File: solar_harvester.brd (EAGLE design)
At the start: 100 x 80 mm, 63 parts, among them U1 BQ25505, U2 TPS61322XA, U3 TPS61322XA, U4 MAX17040, U5 INA226

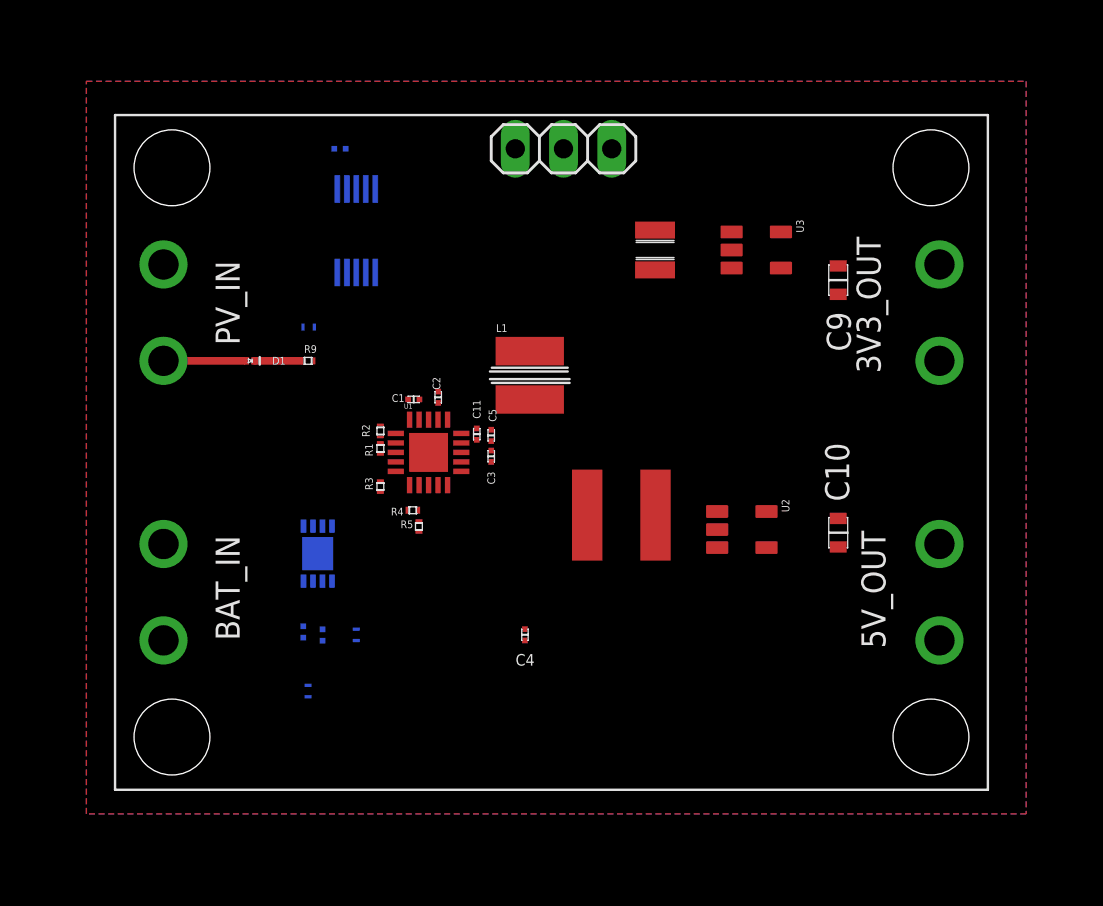
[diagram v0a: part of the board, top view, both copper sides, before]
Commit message: bq25505, both tps622, max17004 routed
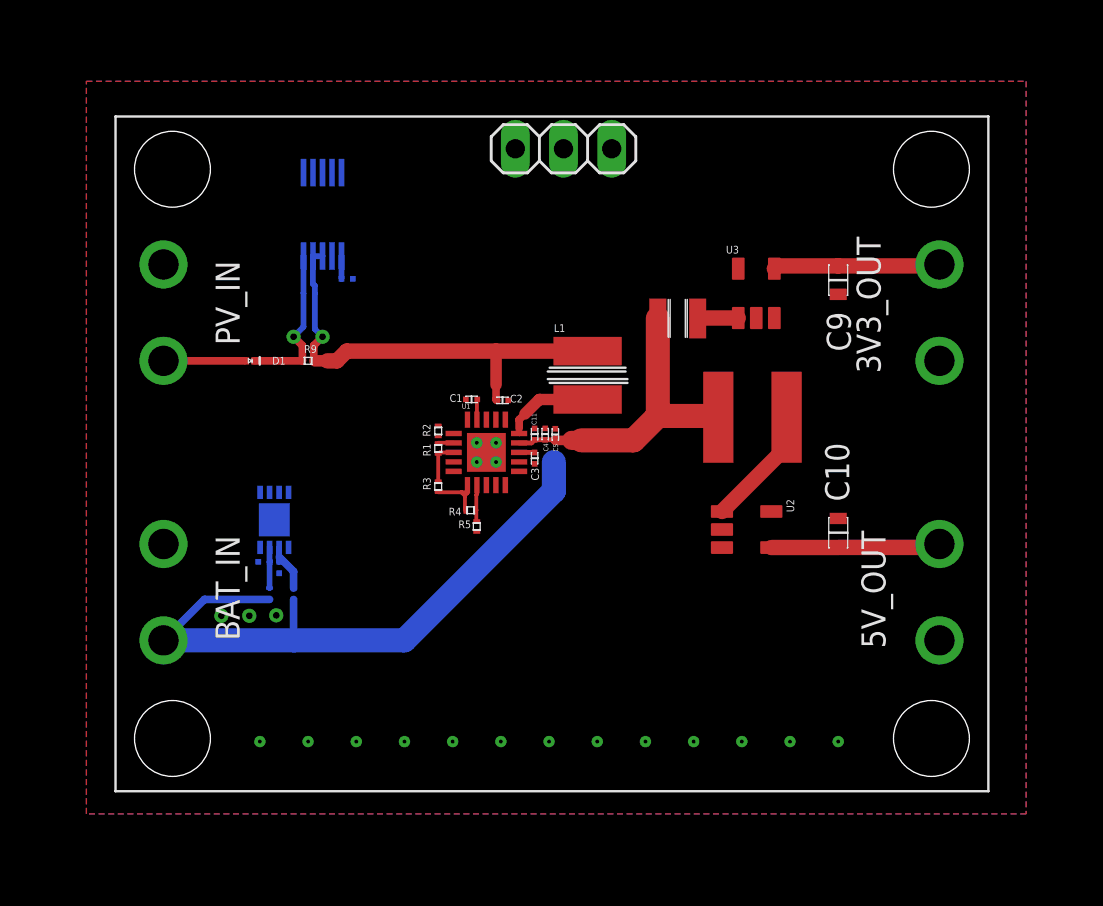
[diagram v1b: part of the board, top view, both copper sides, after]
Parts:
- added U$29: LOUT, vrlib_com_symbols:LOUT_FOOTPRINT
- C11: value 4u7 -> 10u
- C4: value 10u -> 4u7
- moved C4 10.6 mm to (35.4, 31.4)
- moved L2 8.62 mm to (46.3, 32.3)
- moved C8 6.87 mm to (24.9, 39.6)
- moved R7 5.52 mm to (20.8, 23.0)
- moved C7 4.24 mm to (20.5, 24.7), turned to 90 degrees
- moved C6 4.23 mm to (21.3, 24.4)
- moved R6 3.95 mm to (22.1, 23.0)
- moved L3 3.80 mm to (42.3, 37.5), turned to 90 degrees
- moved C2 3.39 mm to (33.1, 33.2), turned to 90 degrees
- moved C5 3.38 mm to (35.9, 31.4)
- moved C11 3.05 mm to (34.8, 31.4)
- moved L1 3.05 mm to (37.6, 34.5)
- moved R4 3.05 mm to (31.4, 27.4)
- moved U1 3.05 mm to (32.3, 30.5)
- moved C1 3.05 mm to (31.5, 33.3)
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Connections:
- removed net GND1: C6.2, C7.2, C8.2, U4.1, U4.4, U4.5, U4.6, U4.9, U5.1, U5.2, U5.7
- removed net VSTOR: C11.1, C5.1, C8.1, U1.19, U1.3, U5.6
- new net VCC: C11.1, C4.1, C5.1, C8.1, L2.1, L3.1, U1.19, U1.3, U5.6
- net GND: now also C6.2, C7.2, C8.2, U4.1, U4.4, U4.5, U4.6, U4.9, U5.1, U5.2, U5.7
- net VIN_BAT: no longer C4.1, L2.1, L3.1
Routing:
- net VIN_BAT: track 0.00 -> 34.8 mm
- net PVIN_AN: track 0.00 -> 23.6 mm, vias 0 -> 1
- net VCC: track 0.00 -> 17.5 mm
- net VDD3V3: track 0.00 -> 8.69 mm
- net VDD5: track 0.00 -> 8.60 mm
- net PVIN: track 2.55 -> 8.48 mm, vias 0 -> 1
- net N$11: track 0.00 -> 5.76 mm
- net N$1: track 0.00 -> 4.77 mm
- net N$5: track 0.00 -> 3.19 mm
- net N$8: track 0.00 -> 2.71 mm
- net N$3: track 0.00 -> 2.26 mm
- net N$10: track 0.00 -> 2.15 mm
- net N$7: track 0.00 -> 2.14 mm
- net N$6: track 0.00 -> 1.90 mm
- net N$2: track 0.00 -> 1.08 mm
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- added copper zone on layer 16, net GND
- removed copper zone on layer 16, net GND2

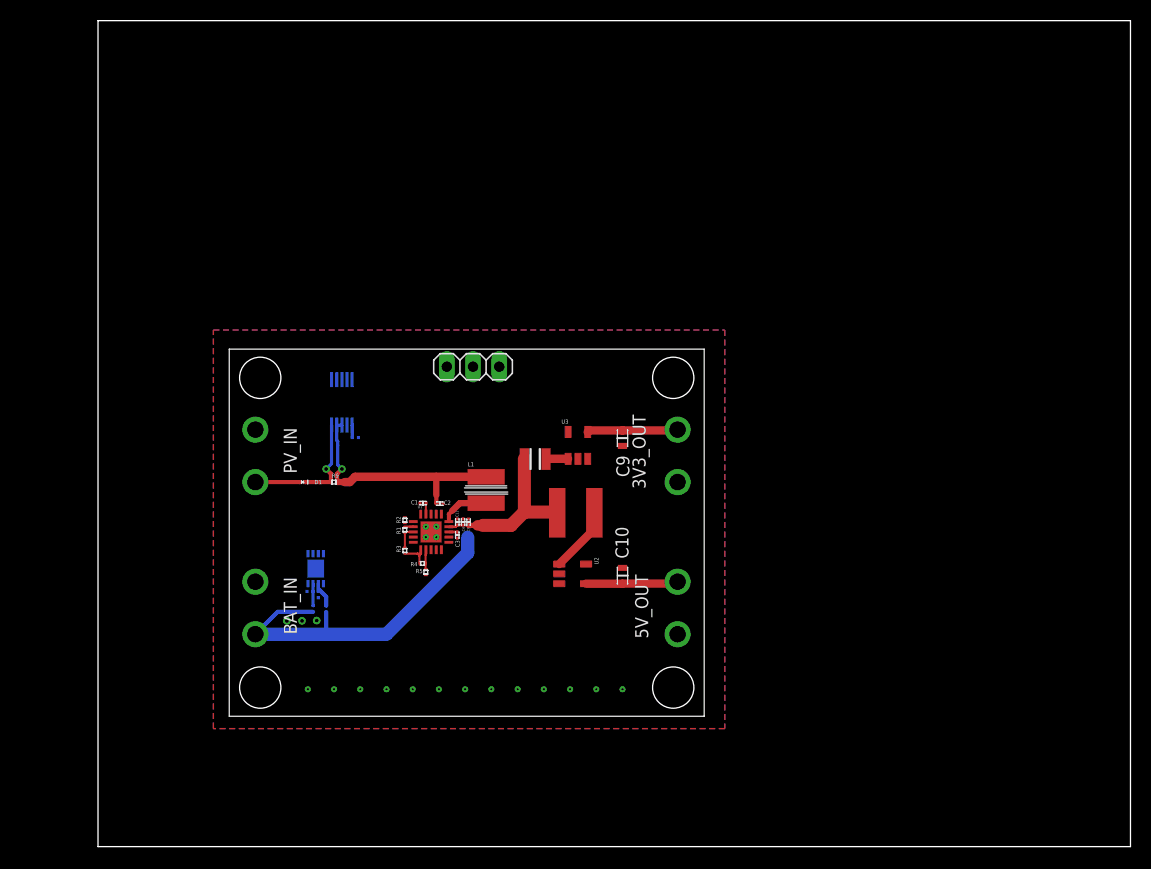
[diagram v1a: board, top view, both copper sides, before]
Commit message: routing complete without battery under-voltage protection
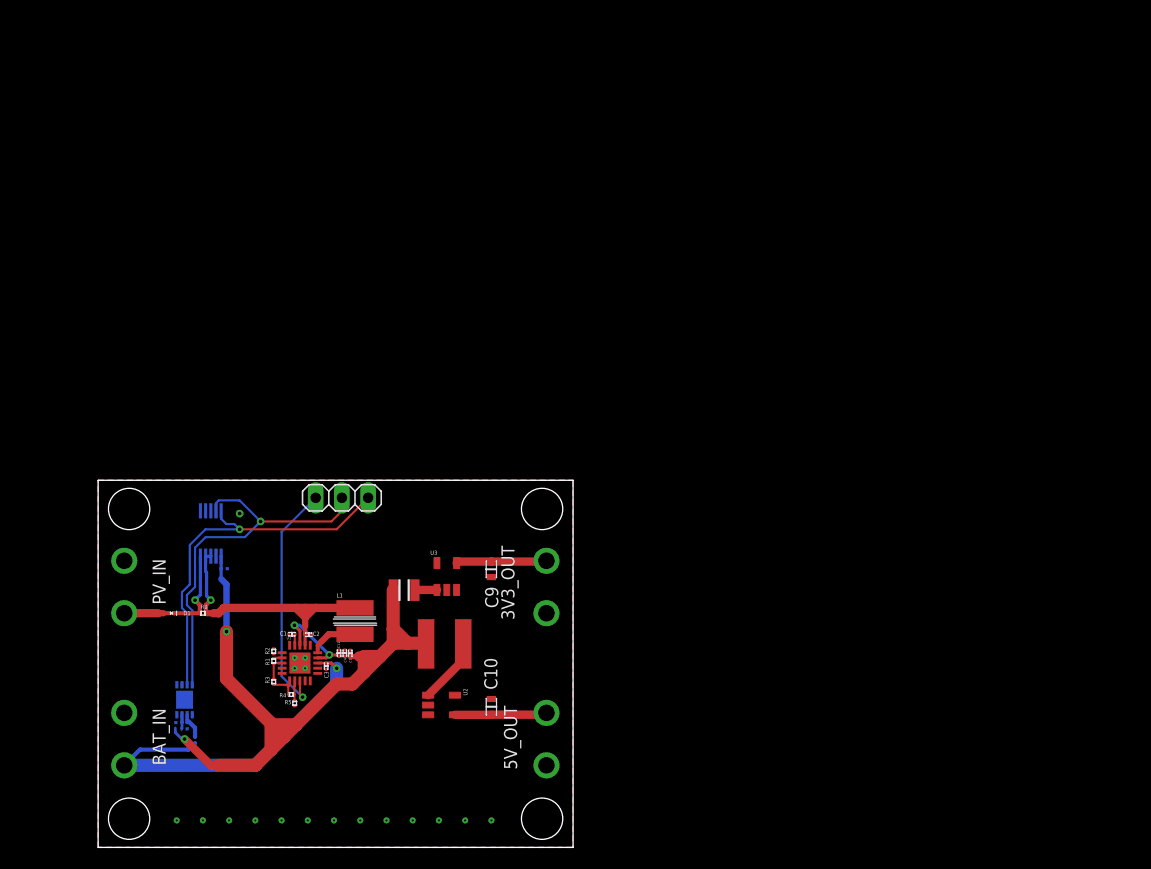
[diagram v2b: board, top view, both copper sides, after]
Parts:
- removed U$1, U$11, U$13, U$14, U$15, U$16, U$17, U$18, U$2, U$21, U$22, U$23, U$24, U$25, U$26, U$27, U$29, U$3, U$5, U$7, U$9: LOUT, vrlib_com_symbols:LOUT_FOOTPRINT
- removed U$10, U$12, U$19, U$20, U$28, U$4, U$6, U$8: GND, vrlib_com_symbols:GND_FOOTPRINT
- moved 5V_OUT 18.0 mm to (43.4, 10.4)
- moved B1 18.0 mm to (23.0, 17.7)
- moved C3 18.0 mm to (22.1, 17.5)
- moved C8 18.0 mm to (12.2, 26.9)
- moved JP1 18.0 mm to (23.6, 33.8)
- moved L3 18.0 mm to (29.6, 24.8)
- moved R8 18.0 mm to (10.2, 26.2)
- moved U1 18.0 mm to (19.6, 17.8)
- moved U3 18.0 mm to (33.8, 26.2)
- moved 3V3_OUT 18.0 mm to (43.4, 25.1)
- moved BAT_IN 18.0 mm to (2.54, 10.4)
- moved C1 18.0 mm to (18.8, 20.6)
- moved C2 18.0 mm to (20.4, 20.5)
- moved C6 18.0 mm to (8.64, 11.7)
- moved C7 18.0 mm to (7.84, 12.0)
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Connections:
- net VCC: now also R7.2
- net VIN_BAT: no longer R7.2
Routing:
- net VCC: track 17.5 -> 77.3 mm, vias 0 -> 4
- net I2C_SDA: track 0.00 -> 36.8 mm, vias 0 -> 1
- net I2C_SCL: track 0.00 -> 36.2 mm, vias 0 -> 1
- net VBAT_OK: track 0.00 -> 23.2 mm, vias 0 -> 1
- net PVIN_AN: track 23.6 -> 27.5 mm
- net N$7: track 2.14 -> 1.36 mm
- net VIN_BAT: track 34.8 -> 35.1 mm, vias 0 -> 1
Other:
- board size 100 x 80 mm -> 46 x 35.6 mm

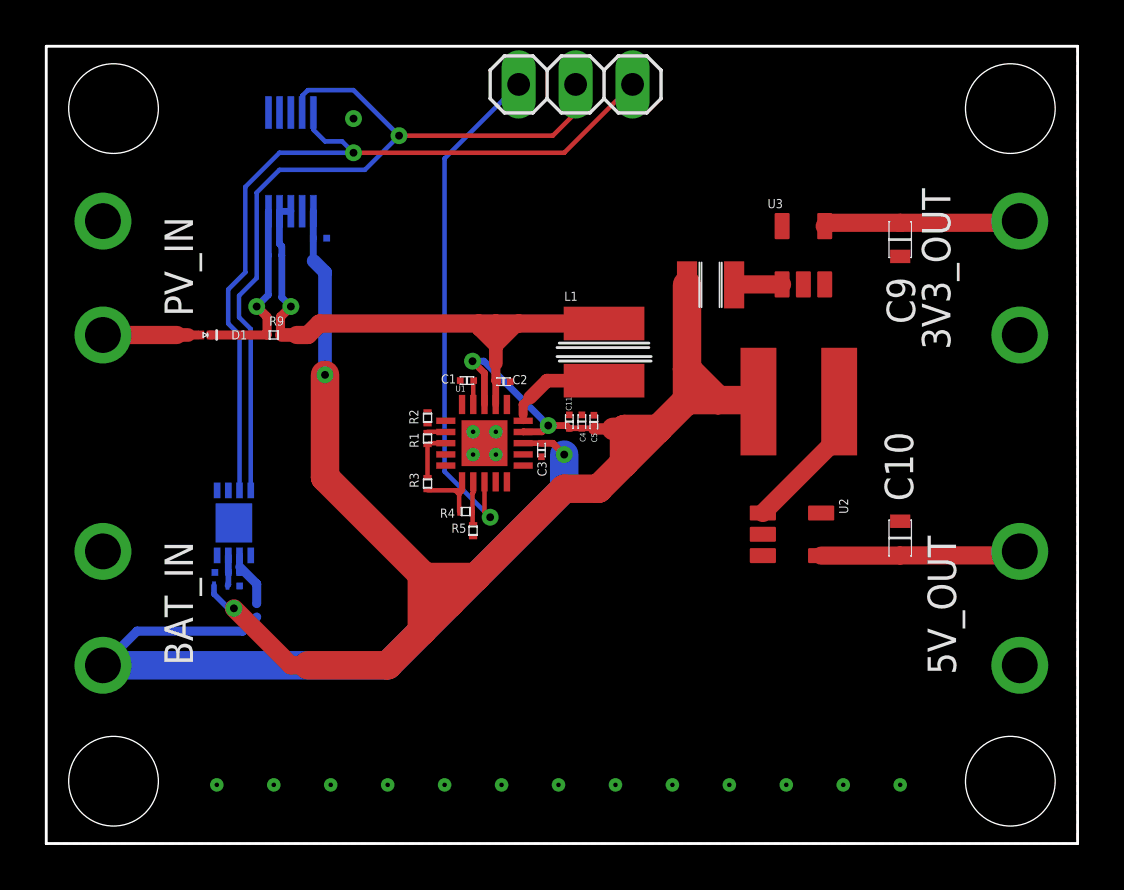
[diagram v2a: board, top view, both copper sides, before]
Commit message: resized board, routing almost finished
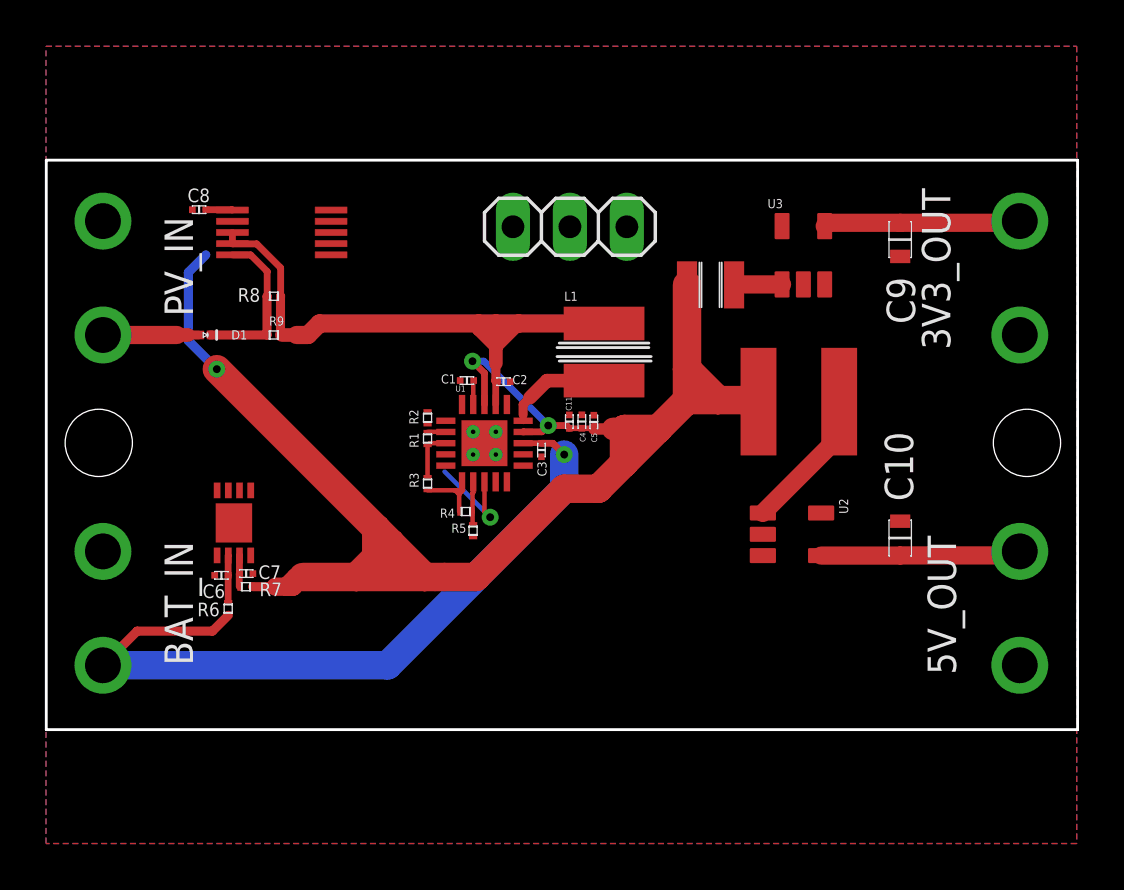
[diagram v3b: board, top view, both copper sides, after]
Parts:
- moved JP1 6.36 mm to (23.4, 27.4)
- moved C8 5.54 mm to (6.83, 28.2), flipped to the top
- moved U5 3.18 mm to (10.5, 27.2), flipped to the top, turned to 90 degrees
- moved R8 1.83 mm to (10.2, 24.3), flipped to the top, turned to 270 degrees
- moved R6 1.27 mm to (8.13, 10.4), flipped to the top
- moved R7 1.12 mm to (8.92, 11.4), flipped to the top
- moved C7 1.09 mm to (8.93, 12.0), flipped to the top
- moved C6 0.83 mm to (7.83, 11.9), flipped to the top, turned to 270 degrees
- flipped U4 to the top
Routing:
- net I2C_SDA: track 36.8 -> 0.00 mm, vias 1 -> 0
- net I2C_SCL: track 36.2 -> 0.00 mm, vias 1 -> 0
- net VBAT_OK: track 23.2 -> 4.56 mm
- net VCC: track 77.3 -> 72.8 mm, vias 4 -> 3
- net VIN_BAT: track 35.1 -> 33.9 mm
- net PVIN: track 8.48 -> 7.24 mm, vias 1 -> 0
- net N$8: track 2.71 -> 2.08 mm
- net PVIN_AN: track 27.5 -> 27.1 mm, vias 1 -> 0
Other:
- board size 46 x 35.6 mm -> 46 x 25.4 mm
